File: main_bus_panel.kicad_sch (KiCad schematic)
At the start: 30 parts

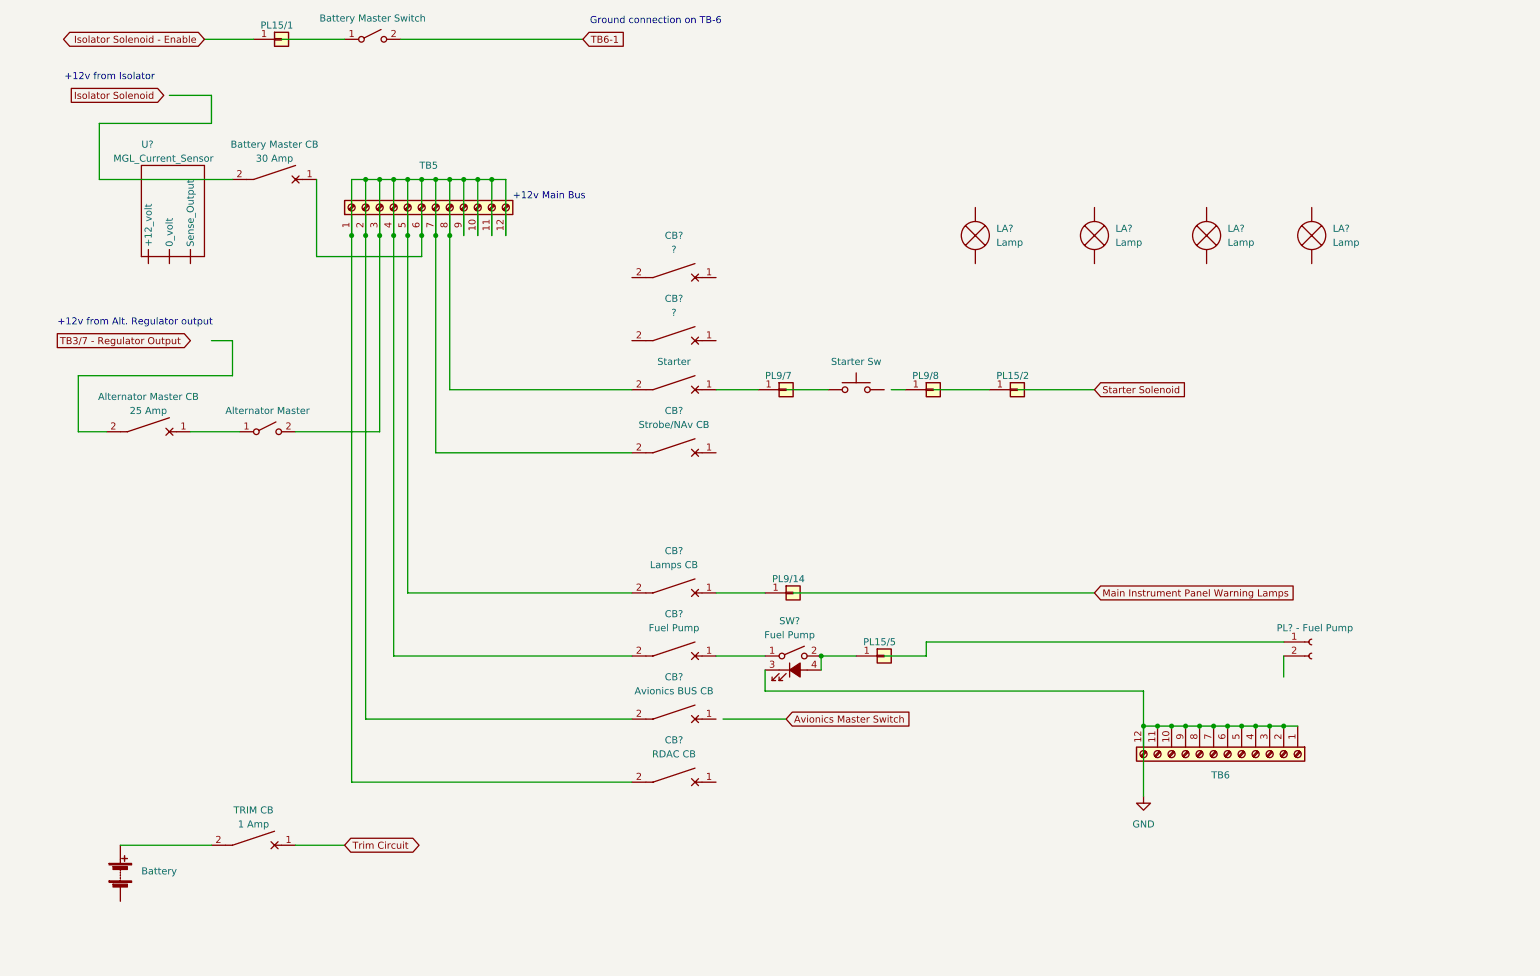
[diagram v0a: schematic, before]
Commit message: Added Trim Circuit and Avionics Bus
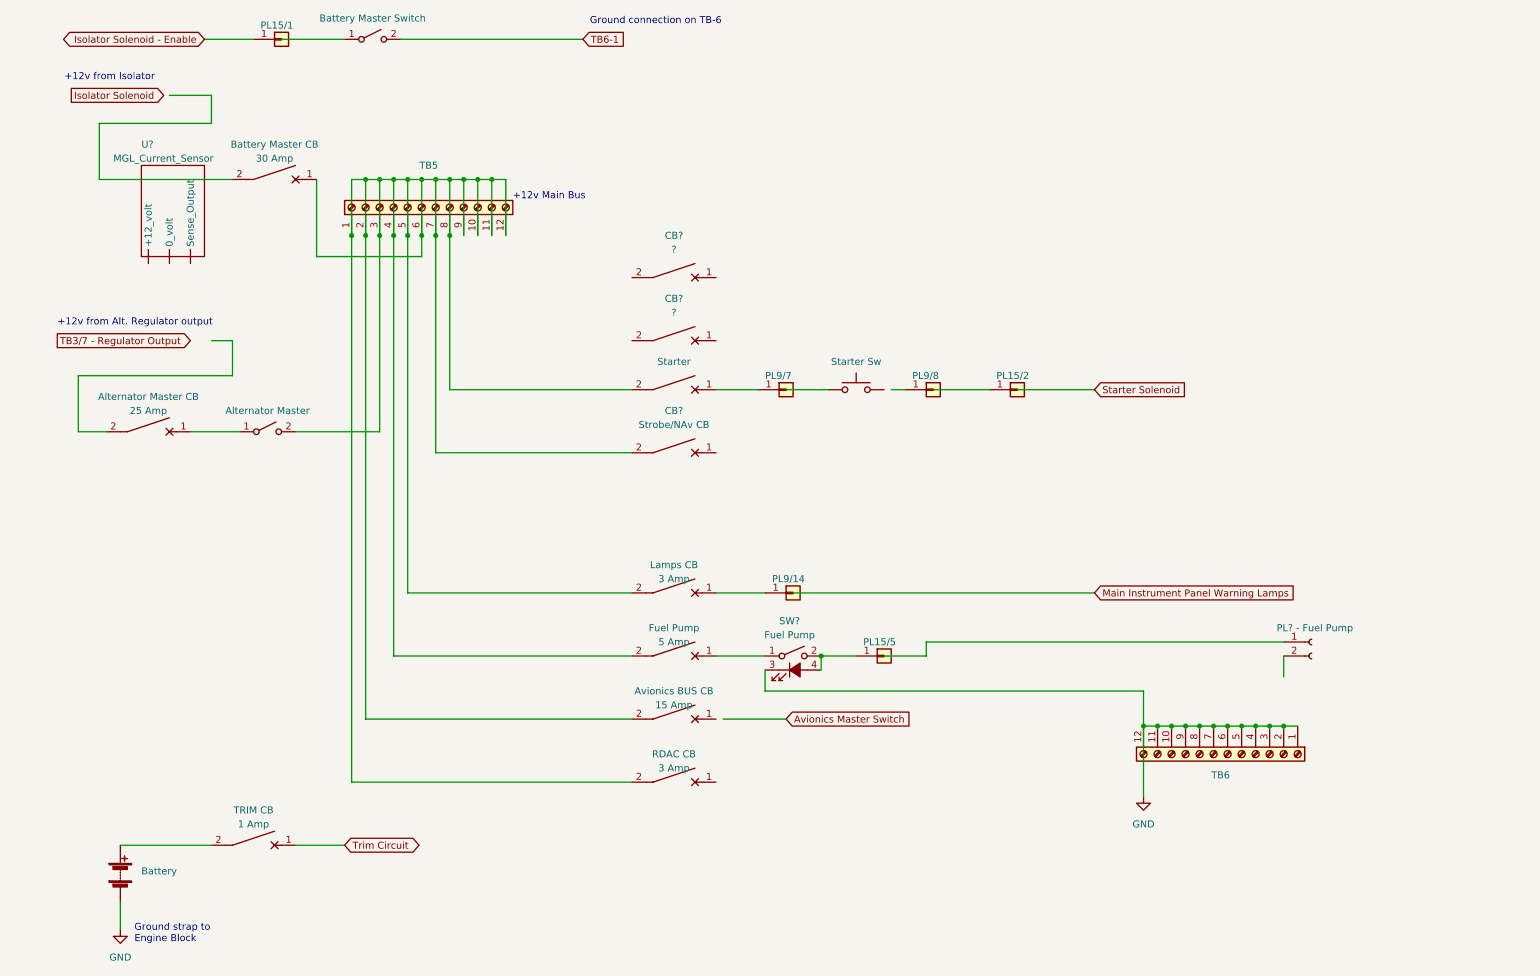
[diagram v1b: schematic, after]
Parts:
- removed LA? (x4): Lamp, symbol Device:Lamp
- CB?: Rating (none) -> 5 Amp
- CB? (x2): Rating (none) -> 3 Amp
- CB?: Rating (none) -> 15 Amp
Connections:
- net GND: now also BT?.2 (-)
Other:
- note added: "Ground strap to Engine Block"
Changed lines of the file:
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@@
     (stroke (width 0) (type default) (color 0 0 0 0))
   )
+  (wire (pts (xy 29.21 177.8) (xy 29.21 182.88))
+    (stroke (width 0) (type default) (color 0 0 0 0))
+  )
   (wire (pts (xy 121.92 85.09) (xy 88.9 85.09))
     (stroke (width 0) (type default) (color 0 0 0 0))
@@
     (effects (font (size 1.27 1.27)) (justify left bottom))
   )
+  (text "Ground strap to\nEngine Block" (at 31.75 185.42 0)
+    (effects (font (size 1.27 1.27)) (justify left bottom))
+  )
   (text "+12v Main Bus" (at 100.33 50.8 0)
     (effects (font (size 1.27 1.27)) (justify left bottom))
@@
   )
   (symbol (lib_id "Device:CircuitBreaker_1P") (at 129.54 133.35 270) (unit 1)
-    (in_bom yes) (on_board yes) (fields_autoplaced)
-    (property "Reference" "CB?" (id 0) (at 129.54 125.73 90))
+    (in_bom yes) (on_board yes)
+    (property "Reference" "CB?" (id 0) (at 129.54 125.73 90)
+      (effects (font (size 1.27 1.27)) hide)
+    )
     (property "Value" "Fuel Pump" (id 1) (at 129.54 128.27 90))
     (property "Footprint" "" (id 2) (at 129.54 133.35 0)
@@
       (effects (font (size 1.27 1.27)) hide)
     )
+    (property "Rating" "5 Amp" (id 4) (at 129.54 130.81 90))
     (pin "1")
     (pin "2")
@@
     (pin "")
   )
-  (symbol (lib_id "Device:Lamp") (at 245.11 57.15 0) (unit 1)
-    (in_bom yes) (on_board yes) (fields_autoplaced)
-    (property "Reference" "LA?" (id 0) (at 248.92 55.8799 0)
-      (effects (font (size 1.27 1.27)) (justify left))
-    )
-    (property "Value" "Lamp" (id 1) (at 248.92 58.4199 0)
-      (effects (font (size 1.27 1.27)) (justify left))
-    )
-    (property "Footprint" "" (id 2) (at 245.11 54.61 90)
-      (effects (font (size 1.27 1.27)) hide)
-    )
-    (property "Datasheet" "~" (id 3) (at 245.11 54.61 90)
+  (symbol (lib_id "Device:CircuitBreaker_1P") (at 129.54 156.21 270) (unit 1)
+    (in_bom yes) (on_board yes)
+    (property "Reference" "CB?" (id 0) (at 129.54 148.59 90)
       (effects (font (size 1.27 1.27)) hide)
     )
-    (pin "1")
-    (pin "2")
-  )
-  (symbol (lib_id "Device:CircuitBreaker_1P") (at 129.54 156.21 270) (unit 1)
-    (in_bom yes) (on_board yes) (fields_autoplaced)
-    (property "Reference" "CB?" (id 0) (at 129.54 148.59 90))
     (property "Value" "RDAC CB" (id 1) (at 129.54 151.13 90))
     (property "Footprint" "" (id 2) (at 129.54 156.21 0)
@@
       (effects (font (size 1.27 1.27)) hide)
     )
+    (property "Rating" "3 Amp" (id 4) (at 129.54 153.67 90))
     (pin "1")
     (pin "2")
@@
   )
   (symbol (lib_id "Device:CircuitBreaker_1P") (at 129.54 121.92 270) (unit 1)
-    (in_bom yes) (on_board yes) (fields_autoplaced)
-    (property "Reference" "CB?" (id 0) (at 129.54 114.3 90))
+    (in_bom yes) (on_board yes)
+    (property "Reference" "CB?" (id 0) (at 129.54 114.3 90)
+      (effects (font (size 1.27 1.27)) hide)
+    )
     (property "Value" "Lamps CB" (id 1) (at 129.54 116.84 90))
     (property "Footprint" "" (id 2) (at 129.54 121.92 0)
@@
       (effects (font (size 1.27 1.27)) hide)
     )
+    (property "Rating" "3 Amp" (id 4) (at 129.54 119.38 90))
     (pin "1")
     (pin "2")
@@
   )
   (symbol (lib_id "Device:CircuitBreaker_1P") (at 129.54 144.78 270) (unit 1)
-    (in_bom yes) (on_board yes) (fields_autoplaced)
-    (property "Reference" "CB?" (id 0) (at 129.54 137.16 90))
+    (in_bom yes) (on_board yes)
+    (property "Reference" "CB?" (id 0) (at 129.54 137.16 90)
+      (effects (font (size 1.27 1.27)) hide)
+    )
     (property "Value" "Avionics BUS CB" (id 1) (at 129.54 139.7 90))
     (property "Footprint" "" (id 2) (at 129.54 144.78 0)
@@
       (effects (font (size 1.27 1.27)) hide)
     )
-    (pin "1")
-    (pin "2")
-  )
-  (symbol (lib_id "Device:Lamp") (at 184.15 57.15 0) (unit 1)
-    (in_bom yes) (on_board yes) (fields_autoplaced)
-    (property "Reference" "LA?" (id 0) (at 187.96 55.8799 0)
-      (effects (font (size 1.27 1.27)) (justify left))
-    )
-    (property "Value" "Lamp" (id 1) (at 187.96 58.4199 0)
-      (effects (font (size 1.27 1.27)) (justify left))
-    )
-    (property "Footprint" "" (id 2) (at 184.15 54.61 90)
-      (effects (font (size 1.27 1.27)) hide)
-    )
-    (property "Datasheet" "~" (id 3) (at 184.15 54.61 90)
-      (effects (font (size 1.27 1.27)) hide)
-    )
+    (property "Rating" "15 Amp" (id 4) (at 129.54 142.24 90))
     (pin "1")
     (pin "2")
@@
     (pin "2")
   )
-  (symbol (lib_id "Device:Lamp") (at 226.06 57.15 0) (unit 1)
+  (symbol (lib_id "power:GND") (at 29.21 182.88 0) (unit 1)
     (in_bom yes) (on_board yes) (fields_autoplaced)
-    (property "Reference" "LA?" (id 0) (at 229.87 55.8799 0)
-      (effects (font (size 1.27 1.27)) (justify left))
-    )
-    (property "Value" "Lamp" (id 1) (at 229.87 58.4199 0)
-      (effects (font (size 1.27 1.27)) (justify left))
-    )
-    (property "Footprint" "" (id 2) (at 226.06 54.61 90)
+    (property "Reference" "#PWR?" (id 0) (at 29.21 189.23 0)
       (effects (font (size 1.27 1.27)) hide)
     )
-    (property "Datasheet" "~" (id 3) (at 226.06 54.61 90)
-      (effects (font (size 1.27 1.27)) hide)
-    )
-    (pin "1")
-    (pin "2")
-  )
-  (symbol (lib_id "Device:Lamp") (at 205.74 57.15 0) (unit 1)
-    (in_bom yes) (on_board yes) (fields_autoplaced)
-    (property "Reference" "LA?" (id 0) (at 209.55 55.8799 0)
-      (effects (font (size 1.27 1.27)) (justify left))
-    )
-    (property "Value" "Lamp" (id 1) (at 209.55 58.4199 0)
-      (effects (font (size 1.27 1.27)) (justify left))
-    )
-    (property "Footprint" "" (id 2) (at 205.74 54.61 90)
+    (property "Value" "GND" (id 1) (at 29.21 187.96 0))
+    (property "Footprint" "" (id 2) (at 29.21 182.88 0)
       (effects (font (size 1.27 1.27)) hide)
     )
-    (property "Datasheet" "~" (id 3) (at 205.74 54.61 90)
+    (property "Datasheet" "" (id 3) (at 29.21 182.88 0)
       (effects (font (size 1.27 1.27)) hide)
     )
     (pin "1")
-    (pin "2")
   )
   (symbol (lib_id "Device:CircuitBreaker_1P") (at 129.54 64.77 270) (unit 1)

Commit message: Proof reading and snagging updates
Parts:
- removed CB? (x2): ?, symbol Device:CircuitBreaker_1P
- added FB1/1, FB2/1, FB2/2, FB2/3, FB2/4: Fuse, symbol Device:Fuse
- added PL15/3: Conn_01x01, symbol Connector_Generic:Conn_01x01
- CB?: value Fuel Pump -> Fuel Pump CB
- CB?: Rating (none) -> 5 Amp
- CB?: value Starter -> Starter CB; Rating (none) -> 5 Amp
- TB6: symbol Connector:Screw_Terminal_01x12 -> Connector:Screw_Terminal_01x10
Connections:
- net GND: no longer SW?.3 (K), TB6.1 (Pin_1), TB6.10 (Pin_10), TB6.11 (Pin_11), TB6.12 (Pin_12), TB6.2 (Pin_2), TB6.3 (Pin_3), TB6.4 (Pin_4), TB6.5 (Pin_5), TB6.6 (Pin_6), TB6.7 (Pin_7), TB6.8 (Pin_8), TB6.9 (Pin_9)
- net TB1/1: now reaches U?. (Sense_Output)
- net at CB?.1: now also FB2/1.2
- net Ground TB4/9: now reaches J?.2 (Pin_2)
- net at BT?.1 (+): now also FB1/1.1; no longer CB?.2
- net TB6-1 renamed TB6/7
- new net: SW?.3 (K), TB6.10 (Pin_10)
- new net: FB2/1.1, FB2/2.2, FB2/3.2, FB2/4.2
- new net: CB?.2, FB1/1.2, PL15/3.1 (Pin_1)
- new net Battery Master Switch: TB6.7 (Pin_7)
- new net COM Radio: TB6.1 (Pin_1)
- new net Current Sensor: FB2/3.1
- new net ECB: TB6.6 (Pin_6)
- new net EFIS: TB6.3 (Pin_3)
- new net FB2/3: U?. (Sense_Output)
- new net Fuel Flow Sensor: FB2/2.1
- new net Ground TB4/4: U?. (Sense_Output)
- new net RDAC: FB2/4.1
- new net Temp & Pres: TB6.8 (Pin_8)
- new net Transponder: TB6.2 (Pin_2)
- new net Trim: TB6.9 (Pin_9)
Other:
- note added: "FB2"
- note added: "Instrument Module Earth Bus"
- moved on the sheet: CB?, SW?, TB5, U?

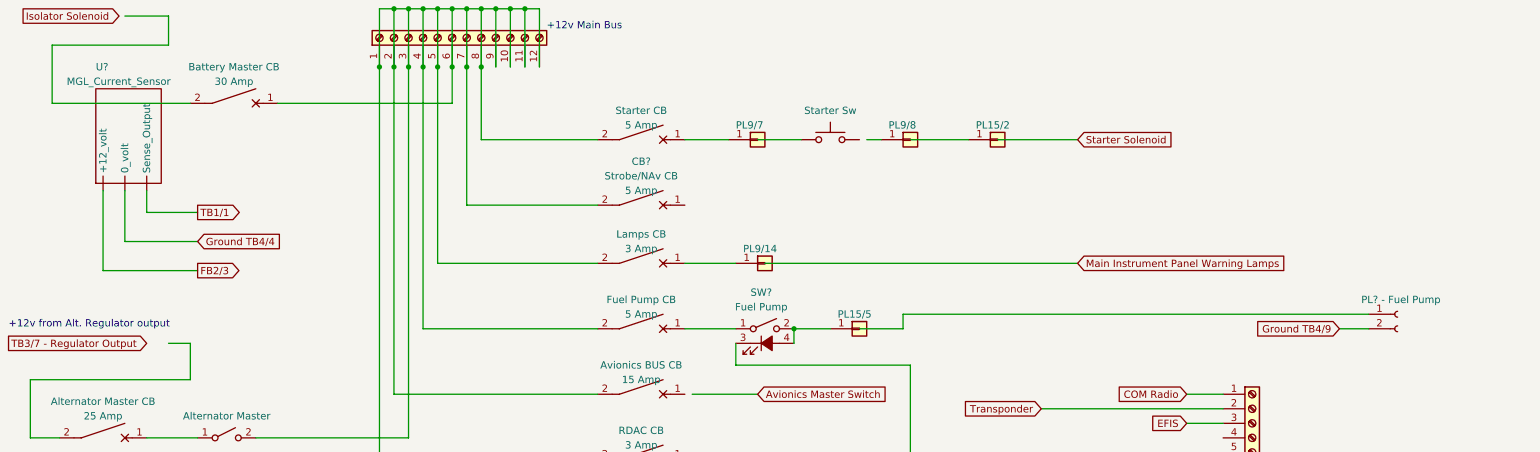
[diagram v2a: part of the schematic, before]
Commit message: Updates from manual validation
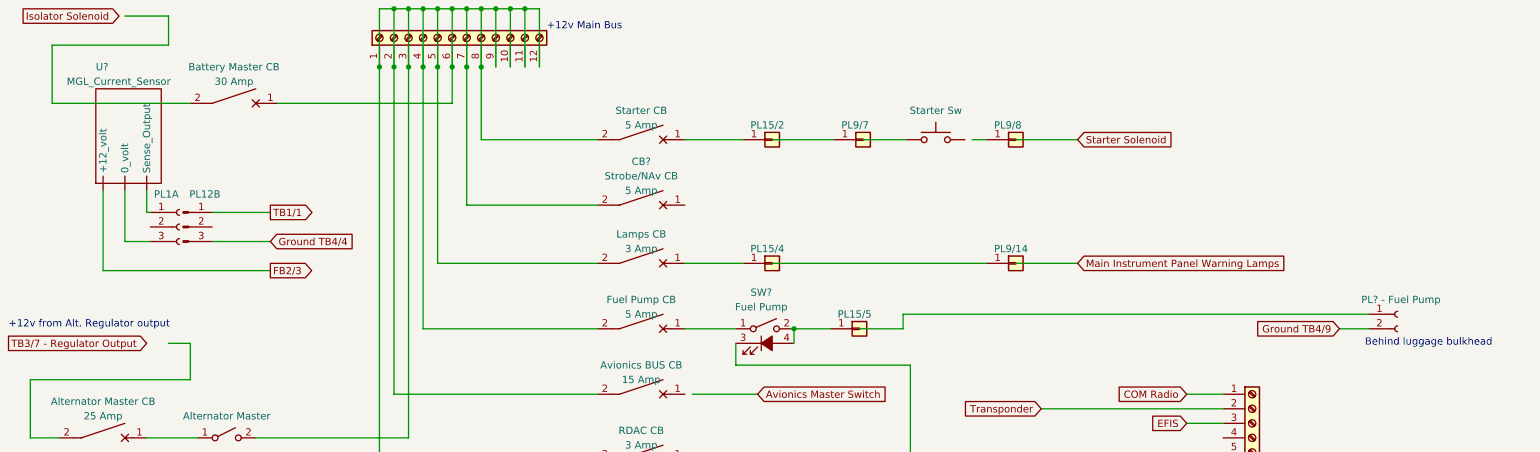
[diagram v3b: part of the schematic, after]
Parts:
- added PL12B: Conn_01x03_Male, symbol Connector:Conn_01x03_Male
- added PL15/4: PL9/14, symbol Connector_Generic:Conn_01x01
- added PL1A: Conn_01x03_Female, symbol Connector:Conn_01x03_Female
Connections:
- net Ground TB4/4: now also PL12B.3 (Pin_3); no longer U?. (Sense_Output)
- net TB1/1: now also PL12B.1 (Pin_1); no longer U?. (Sense_Output)
- net at PL?.1 (Pin_1): no longer CB?.1 (x2)
- net at PL?.1 (Pin_1): now also CB?.1
- new net: PL1A.1 (Pin_1), U?. (Sense_Output)
- new net: PL1A.3 (Pin_3), U?. (Sense_Output)
- new net: CB?.1, PL15/4.1 (Pin_1)
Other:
- note added: "Behind luggage bulkhead"
